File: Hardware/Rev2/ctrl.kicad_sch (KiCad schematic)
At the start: 51 parts, among them J1 USB_C_Receptacle_USB2.0_16P, J2 Conn_01x09, J3 Micro_SD_Card_Det1, J4 Conn_02x04_Odd_Even, J5 SSD1306 OLED, SW1 SW_Push, SW2 SW_Push, U12 74LS125, U13 74LS125, U14 74LS125, U15 ESP32-S3-WROOM-1, U16 USBLC6-2SC6, U17 XC6220B331MR

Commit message: rev.2c revised PCB layout, final
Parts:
- R198, R199, R200, R201, R202, R203, R204, R207, R210, R211, R212, R213, R214, R215: MPN C2930231 -> C15401
- R208, R209: value 220R -> 470R; MPN C2907127 -> C23179
- R216: value 220R -> 470R; MPN C2907127 -> C2907127
- U12, U13, U14: MPN C93012 -> C5138994
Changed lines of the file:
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@@
 			)
 		)
-		(property "MPN" "C2930231"
+		(property "MPN" "C15401"
 			(at 181.61 45.72 90)
 			(effects
@@
 			)
 		)
-		(property "MPN" "C2930231"
+		(property "MPN" "C15401"
 			(at 224.79 71.12 90)
 			(effects
@@
 			)
 		)
-		(property "MPN" "C93012"
+		(property "MPN" "C5138994"
 			(at 172.72 76.2 0)
 			(effects
@@
 			)
 		)
-		(property "MPN" "C2930231"
+		(property "MPN" "C15401"
 			(at 267.97 71.12 90)
 			(effects
@@
 			)
 		)
-		(property "MPN" "C2930231"
+		(property "MPN" "C15401"
 			(at 40.64 95.25 90)
 			(effects
@@
 			)
 		)
-		(property "MPN" "C2930231"
+		(property "MPN" "C15401"
 			(at 134.62 39.37 90)
 			(effects
@@
 			)
 		)
-		(property "MPN" "C93012"
+		(property "MPN" "C5138994"
 			(at 166.37 118.11 0)
 			(effects
@@
 			)
 		)
-		(property "MPN" "C93012"
+		(property "MPN" "C5138994"
 			(at 259.08 50.8 0)
 			(effects
@@
 			)
 		)
-		(property "MPN" "C93012"
+		(property "MPN" "C5138994"
 			(at 259.08 25.4 0)
 			(effects
@@
 			)
 		)
-		(property "MPN" "C2930231"
+		(property "MPN" "C15401"
 			(at 224.79 45.72 90)
 			(effects
@@
 			)
 		)
-		(property "MPN" "C2930231"
+		(property "MPN" "C15401"
 			(at 134.62 34.29 90)
 			(effects
@@
 			)
 		)
-		(property "Value" "220R"
+		(property "Value" "470R"
 			(at 75.438 155.448 90)
 			(effects
@@
 			)
 		)
-		(property "MPN" " C2907127"
+		(property "MPN" "C23179"
 			(at 71.12 157.48 90)
 			(effects
@@
 			)
 		)
-		(property "Value" "220R"
+		(property "Value" "470R"
 			(at 75.438 144.018 90)
 			(effects
@@
 			)
 		)
-		(property "MPN" " C2907127"
+		(property "MPN" "C2907127"
 			(at 71.12 146.05 90)
 			(effects
@@
 			)
 		)
-		(property "Value" "220R"
+		(property "Value" "470R"
 			(at 75.438 150.368 90)
 			(effects
@@
 			)
 		)
-		(property "MPN" " C2907127"
+		(property "MPN" "C23179"
 			(at 71.12 152.4 90)
 			(effects
@@
 			)
 		)
-		(property "MPN" "C93012"
+		(property "MPN" "C5138994"
 			(at 215.9 50.8 0)
 			(effects
@@
 			)
 		)
-		(property "MPN" "C93012"
+		(property "MPN" "C5138994"
 			(at 186.69 118.11 0)
 			(effects
@@
 			)
 		)
-		(property "MPN" "C2930231"
+		(property "MPN" "C15401"
 			(at 134.62 36.83 90)
 			(effects
@@
 			)
 		)
-		(property "MPN" "C2930231"
+		(property "MPN" "C15401"
 			(at 134.62 31.75 90)
 			(effects
@@
 			)
 		)
-		(property "MPN" "C93012"
+		(property "MPN" "C5138994"
 			(at 172.72 50.8 0)
 			(effects
@@
 			)
 		)
-		(property "MPN" "C2930231"
+		(property "MPN" "C15401"
 			(at 181.61 71.12 90)
 			(effects
@@
 			)
 		)
-		(property "MPN" "C2930231"
+		(property "MPN" "C15401"
 			(at 267.97 45.72 90)
 			(effects
@@
 			)
 		)
-		(property "MPN" "C2930231"
+		(property "MPN" "C15401"
 			(at 40.64 125.73 90)
 			(effects
@@
 			)
 		)
-		(property "MPN" "C2930231"
+		(property "MPN" "C15401"
 			(at 134.62 29.21 90)
 			(effects
@@
 			)
 		)
-		(property "MPN" "C93012"
+		(property "MPN" "C5138994"
 			(at 215.9 76.2 0)
 			(effects
@@
 			)
 		)
-		(property "MPN" "C93012"
+		(property "MPN" "C5138994"
 			(at 259.08 76.2 0)
 			(effects
@@
 			)
 		)
-		(property "MPN" "C93012"
+		(property "MPN" "C5138994"
 			(at 172.72 25.4 0)
 			(effects
@@
 			)
 		)
-		(property "MPN" "C93012"
+		(property "MPN" "C5138994"
 			(at 146.05 118.11 0)
 			(effects
@@
 			)
 		)
-		(property "MPN" "C93012"
+		(property "MPN" "C5138994"
 			(at 215.9 25.4 0)
 			(effects
@@
 			)
 		)
-		(property "MPN" "C2930231"
+		(property "MPN" "C15401"
 			(at 134.62 26.67 90)
 			(effects

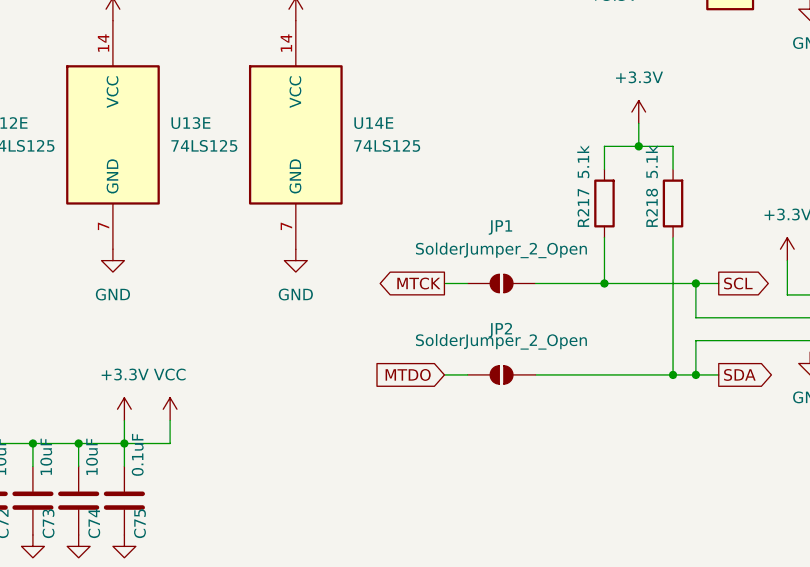
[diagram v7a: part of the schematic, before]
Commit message: add OLED driver and rewire SCL to MTDI/GPIO41 for stability
turns out GPIO39 cannot be used due to PSRAM interference - will need to bodge remaining Rev.2C boards
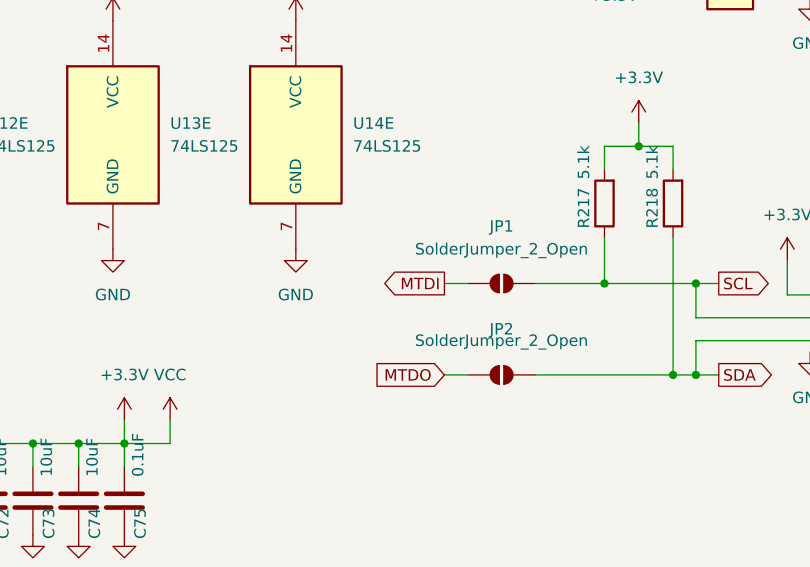
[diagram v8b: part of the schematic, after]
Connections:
- net MTCK: no longer JP1.1 (A)
- net MTDI: now also JP1.1 (A)
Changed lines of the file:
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@@
 		)
 	)
-	(global_label "MTCK"
+	(global_label "MTDI"
 		(shape output)
 		(at 203.2 134.62 180)
@@
 		)
 		(property "Intersheetrefs" "${INTERSHEET_REFS}"
-			(at 195.2558 134.62 0)
+			(at 195.921 134.62 0)
 			(effects
 				(font
